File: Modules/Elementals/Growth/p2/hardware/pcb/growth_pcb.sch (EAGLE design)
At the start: 20 parts, among them J1 EURO_POWER, J2 WQP-PJ398SM6, J3 WQP-PJ398SM6, J4 WQP-PJ398SM6, J5 WQP-PJ398SM6, U1 TL072P

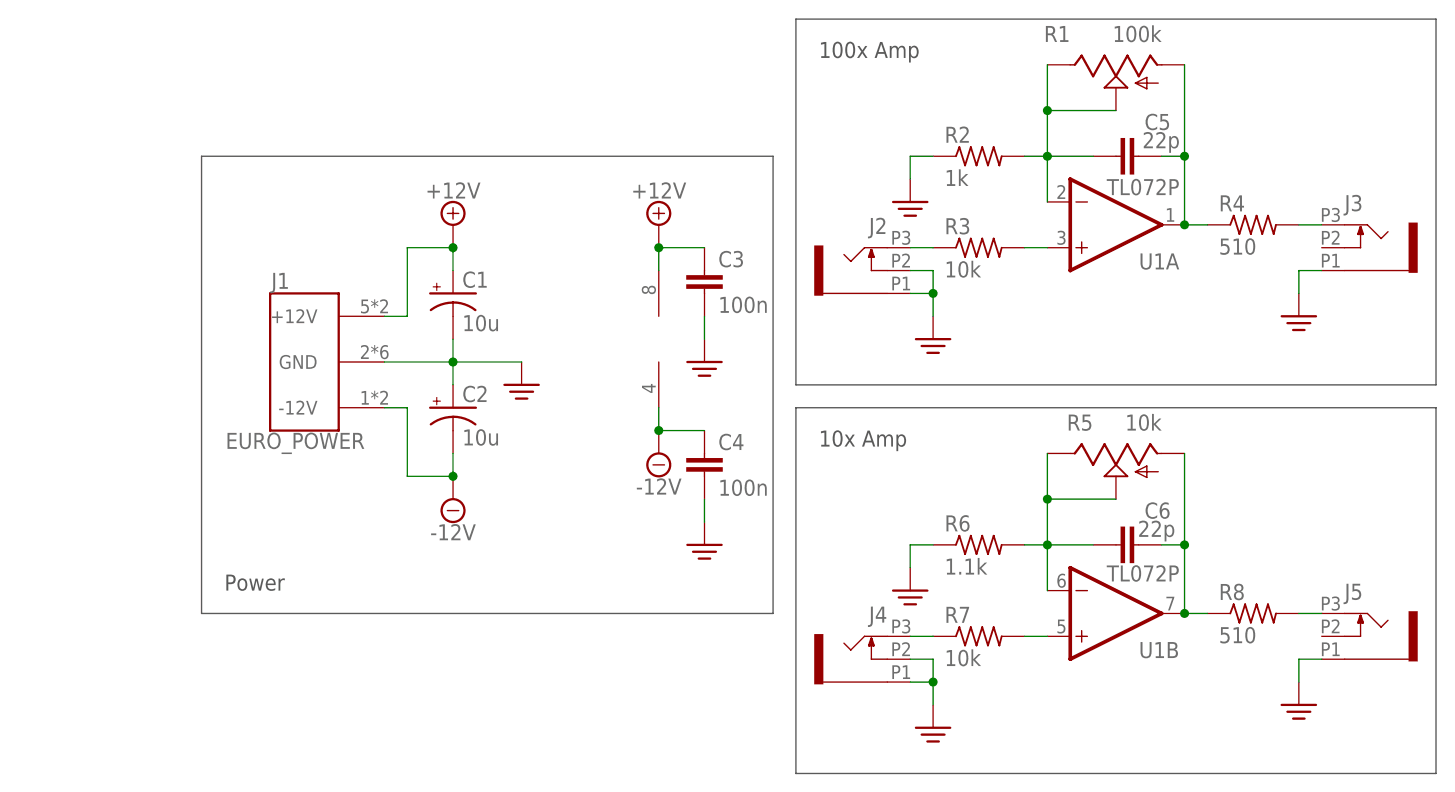
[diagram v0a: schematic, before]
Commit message: New standard power input block on Growth V2
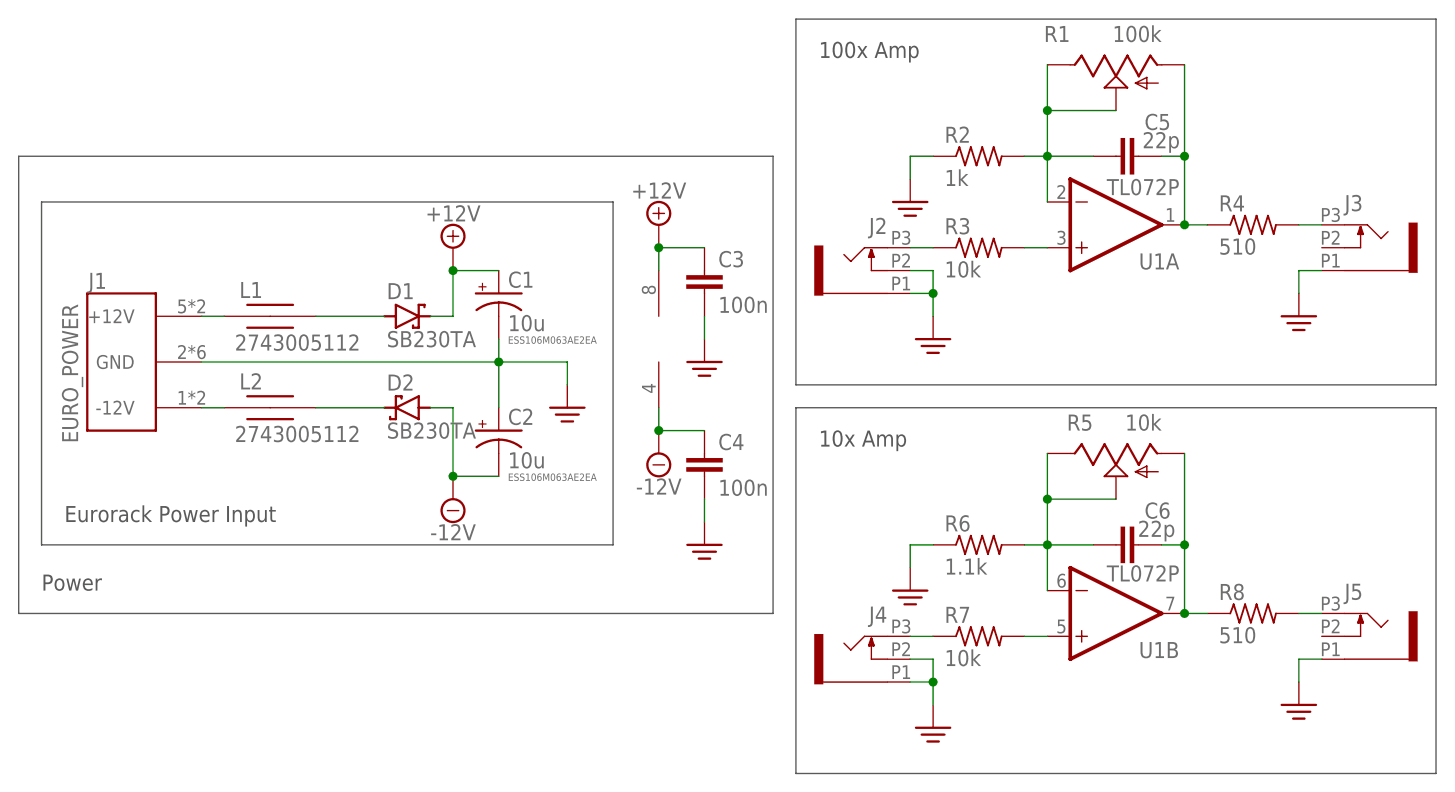
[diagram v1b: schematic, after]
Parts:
- added D1, D2: SB230TA, SonicAthame:SCHOTTKY_THT
- added L1, L2: 2743005112, SonicAthame:FERRITE_THT
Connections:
- new net N$15: D1.A, L1.P$2
- new net N$16: D2.C, L2.P$2
- new net N$17: J1.-12V, L2.P$1
- new net N$18: J1.+12V, L1.P$1
- net +12V: now also D1.C; no longer J1.+12V
- net -12V: now also D2.A; no longer J1.-12V
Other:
- note added: "ESS106M063AE2EA"
- note added: "Eurorack Power Input"
- moved on the sheet: C1, C2, J1

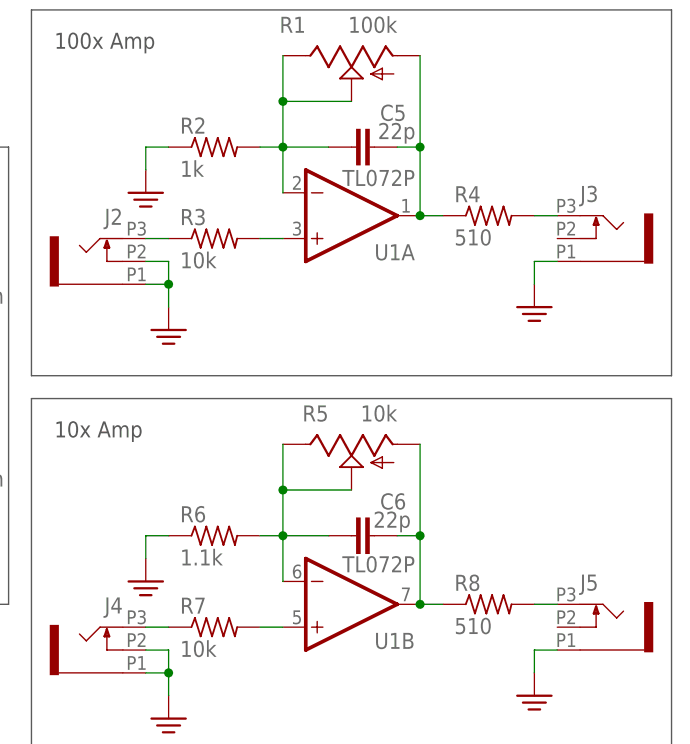
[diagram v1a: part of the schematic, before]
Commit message: Finished elemental growth p2 PCB
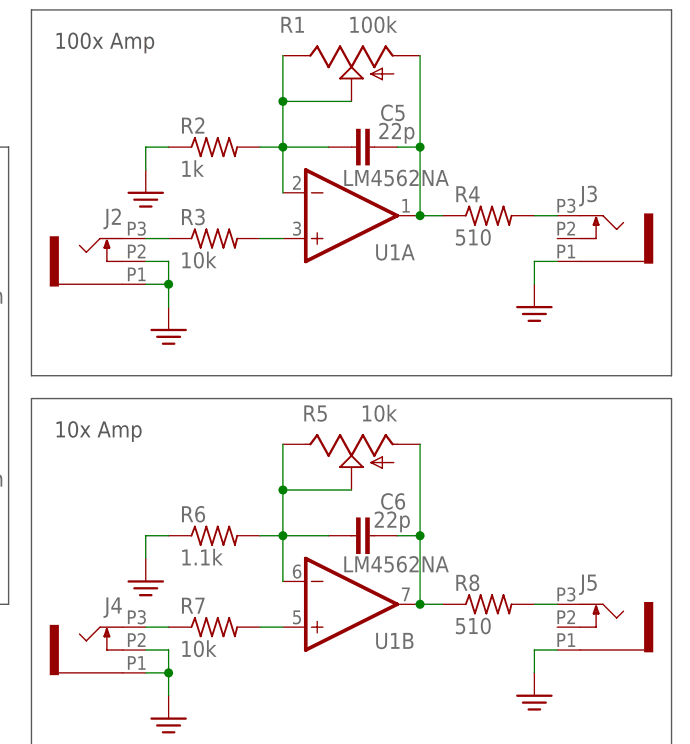
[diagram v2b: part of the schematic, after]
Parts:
- U1: value TL072P -> LM4562NA
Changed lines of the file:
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@@
 </classes>
 <parts>
-<part name="U1" library="SonicAthame" library_urn="urn:adsk.eagle:library:22327399" deviceset="TL072" device="P" package3d_urn="urn:adsk.eagle:package:16409/2"/>
+<part name="U1" library="SonicAthame" library_urn="urn:adsk.eagle:library:22327399" deviceset="TL072" device="P" package3d_urn="urn:adsk.eagle:package:16409/2" value="LM4562NA"/>
 <part name="SUPPLY4" library="SonicAthame" library_urn="urn:adsk.eagle:library:22327399" deviceset="+12V" device=""/>
 <part name="SUPPLY5" library="SonicAthame" library_urn="urn:adsk.eagle:library:22327399" deviceset="-12V" device=""/>
